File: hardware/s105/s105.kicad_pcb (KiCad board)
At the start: 2 copper layers, 86 x 159 mm, 367 parts, among them J1 Conn_01x06, P1 368255-2, Q1 BC847C, Q10 BC847C, Q11 BC847C, Q12 BC847C, Q13 BC847C, Q14 BC847C, Q15 BC847C, Q16 BC847C, Q17 BC847C, Q2 BC847C, Q20 BC847C, Q21 BC847C, Q22 BC847C, Q23 BC847C, Q3 BC847C, Q4 ., Q5 ., Q6 BC847C, Q7 BC847C, Q9 BC847C, U2 STM32F427VGT6, U4 case only, X1 8MHz 20pF

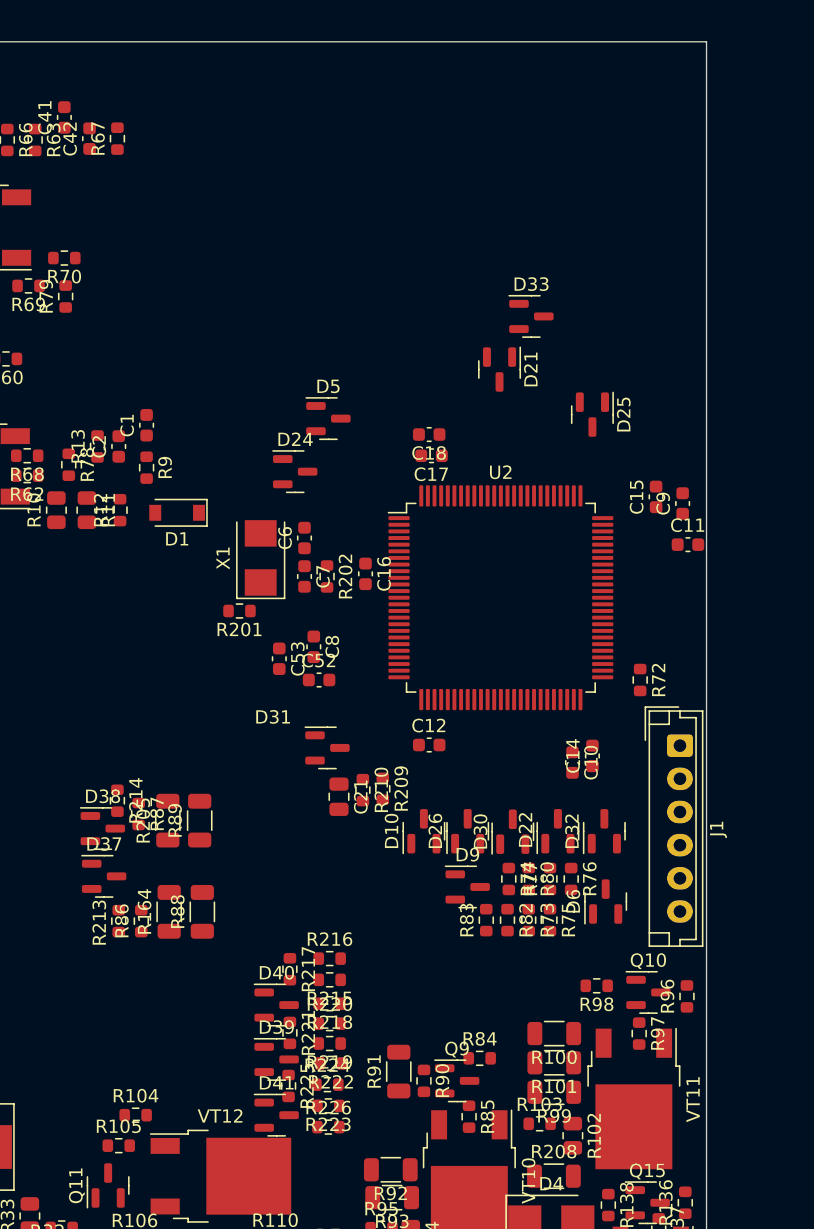
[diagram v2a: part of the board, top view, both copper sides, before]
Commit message: новые модули, продолжение расположения
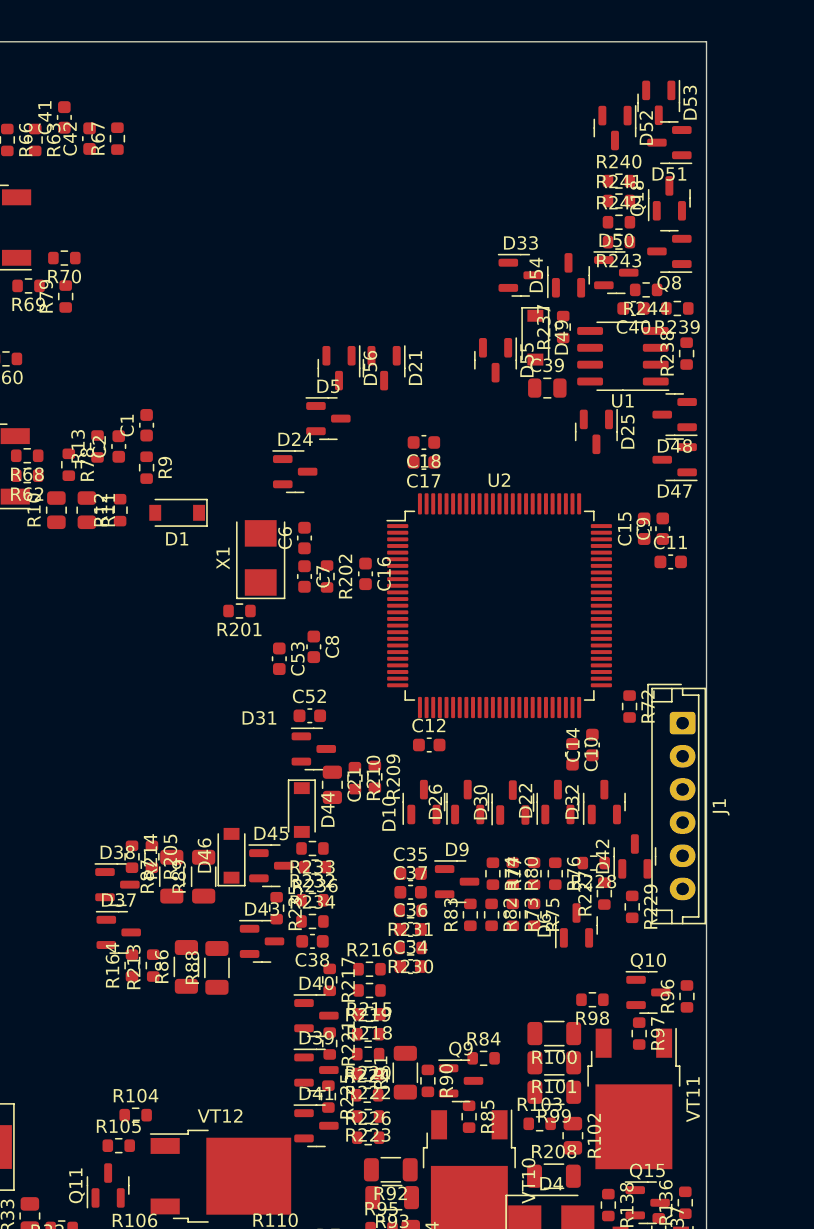
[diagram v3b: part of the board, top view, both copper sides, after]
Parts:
- added C34: 100nF, Capacitor_SMD:C_0603_1608Metric, F.Cu at (113.7, 169.7)
- added C35: 100nF, Capacitor_SMD:C_0603_1608Metric, F.Cu at (113.7, 162.7)
- added C36: 100nF, Capacitor_SMD:C_0603_1608Metric, F.Cu at (113.7, 166.9)
- added C37: 100nF, Capacitor_SMD:C_0603_1608Metric, F.Cu at (113.7, 164.1)
- added C38: 100nF, Capacitor_SMD:C_0603_1608Metric, F.Cu at (106.3, 167.8)
- added C39: C0805, Capacitor_SMD:C_0805_2012Metric, F.Cu at (124.0, 126.1)
- added C40: C0603, Capacitor_SMD:C_0603_1608Metric, F.Cu at (130.5, 120.1)
- added D42: BAV99, Package_TO_SOT_SMD:SOT-23, F.Cu at (130.6, 161.4)
- added D43: BAV99, Package_TO_SOT_SMD:SOT-23, F.Cu at (102.5, 167.8)
- added D44: 1N4148W, Diode_SMD:D_SOD-123, F.Cu at (105.5, 157.9)
- added D45: BAV99, Package_TO_SOT_SMD:SOT-23, F.Cu at (103.2, 162.1)
- added D46: 1N4148W, Diode_SMD:D_SOD-123, F.Cu at (100.2, 161.3)
- added D47: BAV99, Package_TO_SOT_SMD:SOT-23, F.Cu at (133.6, 131.5)
- added D48: BAV99, Package_TO_SOT_SMD:SOT-23, F.Cu at (133.6, 128.1)
- added D49: ., Diode_SMD:D_SOD-123, F.Cu at (123.1, 122.3)
- added D50: BAV99, Package_TO_SOT_SMD:SOT-23, F.Cu at (129.2, 117.4)
- added D51: BAV99, Package_TO_SOT_SMD:SOT-23, F.Cu at (133.2, 107.6)
- added D52: BAV99, Package_TO_SOT_SMD:SOT-23, F.Cu at (129.1, 106.5)
- added D53: BAV99, Package_TO_SOT_SMD:SOT-23, F.Cu at (132.4, 104.6)
- added D54: BAV99, Package_TO_SOT_SMD:SOT-23, F.Cu at (125.6, 117.6)
- added D55: BAV99, Package_TO_SOT_SMD:SOT-23, F.Cu at (120.1, 124.0)
- added D56: BAV99, Package_TO_SOT_SMD:SOT-23, F.Cu at (108.3, 124.6)
- added Q18: BC847C, Package_TO_SOT_SMD:SOT-23, F.Cu at (133.2, 111.8)
- added Q8: BC847C, Package_TO_SOT_SMD:SOT-23, F.Cu at (133.2, 115.8)
- added R227: NM, Resistor_SMD:R_0603_1608Metric, F.Cu at (128.3, 164.2)
- added R228: NM, Resistor_SMD:R_0603_1608Metric, F.Cu at (127.5, 161.9)
- added R229: NM, Resistor_SMD:R_0603_1608Metric, F.Cu at (130.4, 165.2)
- added R230: 3k, Resistor_SMD:R_0603_1608Metric, F.Cu at (113.7, 168.3)
- added R231: 3k, Resistor_SMD:R_0603_1608Metric, F.Cu at (113.7, 165.5)
- added R232: NM, Resistor_SMD:R_0603_1608Metric, F.Cu at (106.3, 164.7)
- added R233: 1k, Resistor_SMD:R_0603_1608Metric, F.Cu at (106.3, 160.8)
- added R234: NM, Resistor_SMD:R_0603_1608Metric, F.Cu at (106.3, 166.3)
- added R235: NM, Resistor_SMD:R_0603_1608Metric, F.Cu at (103.6, 165.3)
- added R236: 1k, Resistor_SMD:R_0603_1608Metric, F.Cu at (106.5, 162.2)
- added R237: 22k, Resistor_SMD:R_0603_1608Metric, F.Cu at (125.2, 121.5)
- added R238: NM, Resistor_SMD:R_0603_1608Metric, F.Cu at (134.5, 123.5)
- added R239: 4.7k, Resistor_SMD:R_0603_1608Metric, F.Cu at (133.8, 120.1)
- added R240: 47, Resistor_SMD:R_0603_1608Metric, F.Cu at (129.4, 110.5)
- added R241: 47, Resistor_SMD:R_0603_1608Metric, F.Cu at (129.4, 112.0)
- added R242: 51k, Resistor_SMD:R_0603_1608Metric, F.Cu at (129.4, 113.6)
- added R243: 33k, Resistor_SMD:R_0603_1608Metric, F.Cu at (129.4, 115.1)
- added R244: 33k, Resistor_SMD:R_0603_1608Metric, F.Cu at (131.4, 118.7)
- added U1: case only, Package_SO:SOIC-8_3.9x4.9mm_P1.27mm, F.Cu at (129.7, 123.7)
- R164, R205: value 3k -> 22k; footprint Resistor_SMD:R_1206_3216Metric -> Resistor_SMD:R_0603_1608Metric
- R201: value R0603 -> 3k
- R219: value 10k -> NM
- R220: value NM -> 10k
- R86, R87: value 22k -> 3k; footprint Resistor_SMD:R_0603_1608Metric -> Resistor_SMD:R_1206_3216Metric
- moved D21 8.70 mm to (111.7, 124.6)
- moved R87 5.35 mm to (95.7, 162.9), turned to 90 degrees
- moved R164 4.92 mm to (92.7, 169.6)
- moved R86 4.84 mm to (96.8, 169.7)
- moved R214 4.37 mm to (92.7, 161.4)
- moved R88 4.37 mm to (99.1, 169.8)
- moved D37 4.37 mm to (91.7, 167.1)
- moved D38 4.37 mm to (91.6, 163.5)
- moved R213 4.24 mm to (94.3, 169.6)
- moved R89 4.24 mm to (98.1, 162.9)
- moved R220 3.70 mm to (110.5, 176.3), turned to 180 degrees
- moved D33 3.20 mm to (122.0, 117.6)
- moved D39 3.10 mm to (106.6, 177.5)
- moved D40 3.10 mm to (106.6, 173.4)
- moved R215 3.10 mm to (110.6, 171.5)
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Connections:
- net /MCU/PC1 renamed /PC1
- C21 pad 1: /MCU/PB1 -> /PB1
- D24 pad 3: /MCU/PE3 -> /PE3
- D25 pad 3: /MCU/PA15 -> /PA15
- D30 pad 3: /MCU/PB10 -> /PB10
- D31 pad 3: /MCU/PB1 -> /PB1
- R164 pad 2: +3.3V -> /PA3
- R205 pad 1: +3.3V -> /CLT
- R205 pad 2: /CLT -> GND
- R209 pad 1: /MCU/PB1 -> /PB1
- R210 pad 1: /MCU/PB1 -> /PB1
- R213 pad 2: /PA3 -> GND
- R216 pad 2: +5V -> +5VD
- R219 pad 1: GND -> /TPS
- R219 pad 2: /TPS -> +5VD
- R220 pad 1: /TPS -> GND
- R220 pad 2: +5V -> /TPS
- R224 pad 2: +5V -> +5VD
- R72 pad 1: /MCU/PB15 -> /PB15
- R74 pad 1: +5V -> +5VD
- R80 pad 1: +5V -> +5VD
- R86 pad 2: GND -> +3.3V
- R87 pad 1: /CLT -> +3.3V
- R87 pad 2: GND -> /CLT
- U2 pad 15: /MCU/PC0 -> /PC0
- U2 pad 25: /MCU/PA2 -> /PA2
- U2 pad 38: /MCU/PE7 -> /PE7
- U2 pad 65: /MCU/PC8 -> /PC8
- U2 pad 68: /MCU/PA9 -> /PA9
- U2 pad 69: /MCU/PA10 -> /PA10

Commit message: заполняем плату дальше
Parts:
- added C44: C0603, Capacitor_SMD:C_0603_1608Metric, F.Cu at (86.6, 163.0)
- added C45: C0603, Capacitor_SMD:C_0603_1608Metric, F.Cu at (83.2, 173.6)
- added C46: C0603, Capacitor_SMD:C_0603_1608Metric, F.Cu at (80.9, 167.1)
- added C47: C0805, Capacitor_SMD:C_0805_2012Metric, F.Cu at (78.1, 161.1)
- added C48: C0603, Capacitor_SMD:C_0603_1608Metric, F.Cu at (71.5, 170.6)
- added C49: C0603, Capacitor_SMD:C_0603_1608Metric, F.Cu at (71.5, 169.2)
- added C50: C1206, Capacitor_SMD:C_1206_3216Metric, F.Cu at (72.3, 167.4)
- added C51: C1206, Capacitor_SMD:C_1206_3216Metric, F.Cu at (72.2, 163.8)
- added C55: C0603, Capacitor_SMD:C_0603_1608Metric, F.Cu at (71.4, 165.6)
- added C64: C0603, Capacitor_SMD:C_0603_1608Metric, F.Cu at (71.4, 160.2)
- added C69: 100nF, Capacitor_SMD:C_0603_1608Metric, F.Cu at (71.4, 158.8)
- added C70: C0603, Capacitor_SMD:C_0603_1608Metric, F.Cu at (71.4, 154.0)
- added C71: C0603, Capacitor_SMD:C_0603_1608Metric, F.Cu at (71.4, 152.6)
- added C72: 100nF, Capacitor_SMD:C_0603_1608Metric, F.Cu at (71.4, 151.3)
- added C73: C0603, Capacitor_SMD:C_0603_1608Metric, F.Cu at (71.4, 149.9)
- added C74: 100nF, Capacitor_SMD:C_0603_1608Metric, F.Cu at (73.8, 153.3)
- added C75: 100nF, Capacitor_SMD:C_0603_1608Metric, F.Cu at (71.4, 146.7)
- added C76: 100nF, Capacitor_SMD:C_0603_1608Metric, F.Cu at (73.0, 145.5)
- added C77: 100nF, Capacitor_SMD:C_0603_1608Metric, F.Cu at (71.4, 144.3)
- added C78: C0603, Capacitor_SMD:C_0603_1608Metric, F.Cu at (71.4, 143.0)
- added C79: 100nF, Capacitor_SMD:C_0603_1608Metric, F.Cu at (71.4, 141.8)
- added C80: C0603, Capacitor_SMD:C_0603_1608Metric, F.Cu at (71.4, 140.5)
- added C81: C0603, Capacitor_SMD:C_0603_1608Metric, F.Cu at (71.4, 139.2)
- added C82: C0603, Capacitor_SMD:C_0603_1608Metric, F.Cu at (73.8, 140.6)
- added C83: C0603, Capacitor_SMD:C_0603_1608Metric, F.Cu at (73.8, 143.5)
- added C84: C0603, Capacitor_SMD:C_0603_1608Metric, F.Cu at (71.4, 137.8)
- added C85: C0603, Capacitor_SMD:C_0603_1608Metric, F.Cu at (71.4, 136.5)
- added C86: C0603, Capacitor_SMD:C_0603_1608Metric, F.Cu at (71.4, 135.2)
- added C87: C0603, Capacitor_SMD:C_0603_1608Metric, F.Cu at (74.3, 133.9)
- added C88: C0603, Capacitor_SMD:C_0603_1608Metric, F.Cu at (73.8, 136.9)
- added C89: C0603, Capacitor_SMD:C_0603_1608Metric, F.Cu at (96.5, 146.7)
- added C90: C0603, Capacitor_SMD:C_0603_1608Metric, F.Cu at (103.7, 155.3)
- added C94: C0603, Capacitor_SMD:C_0603_1608Metric, F.Cu at (97.0, 158.4)
- added Q19: ., Package_TO_SOT_SMD:SOT-23, F.Cu at (76.4, 174.4)
- added R245: 4.7k, Resistor_SMD:R_0603_1608Metric, F.Cu at (85.7, 161.3)
- added R246: 82k, Resistor_SMD:R_0603_1608Metric, F.Cu at (80.4, 174.3)
- added R247: 4.7k, Resistor_SMD:R_0603_1608Metric, F.Cu at (78.5, 166.4)
- added R248: 10k, Resistor_SMD:R_0805_2012Metric, F.Cu at (79.9, 163.3)
- added R249: 10k, Resistor_SMD:R_0805_2012Metric, F.Cu at (78.6, 171.7)
- added R250: 10k, Resistor_SMD:R_0805_2012Metric, F.Cu at (76.4, 163.3)
- added R251: 4.7k, Resistor_SMD:R_0603_1608Metric, F.Cu at (76.9, 164.9)
- added R252: 4.7k, Resistor_SMD:R_0603_1608Metric, F.Cu at (78.7, 169.8)
- added R253: 4.7k, Resistor_SMD:R_0603_1608Metric, F.Cu at (77.0, 168.2)
- added R254: 4.7k, Resistor_SMD:R_0603_1608Metric, F.Cu at (90.5, 172.7)
- added R255: NM, Resistor_SMD:R_0603_1608Metric, F.Cu at (88.6, 172.7)
- added R256: 0, Resistor_SMD:R_0805_2012Metric, F.Cu at (71.7, 173.4)
- added R257: 0, Resistor_SMD:R_0805_2012Metric, F.Cu at (71.6, 161.8)
- added R258: 0, Resistor_SMD:R_0805_2012Metric, F.Cu at (71.6, 148.3)
- added R259: 0, Resistor_SMD:R_0805_2012Metric, F.Cu at (71.6, 155.5)
- added R260: 0, Resistor_SMD:R_0805_2012Metric, F.Cu at (71.6, 157.3)
- added R261: NM, Resistor_SMD:R_0603_1608Metric, F.Cu at (99.4, 146.6)
- added R262: MN, Resistor_SMD:R_0603_1608Metric, F.Cu at (98.6, 148.9)
- added R263: 3k, Resistor_SMD:R_0603_1608Metric, F.Cu at (98.0, 146.6)
- added R264: 3k, Resistor_SMD:R_0603_1608Metric, F.Cu at (96.4, 152.5)
- added R265: MN, Resistor_SMD:R_0603_1608Metric, F.Cu at (104.7, 148.5)
- added R266: MN, Resistor_SMD:R_0603_1608Metric, F.Cu at (100.8, 146.5)
- added R267: MN, Resistor_SMD:R_0603_1608Metric, F.Cu at (101.6, 148.9)
- added R268: MN, Resistor_SMD:R_0603_1608Metric, F.Cu at (102.3, 146.5)
- added R269: 10k, Resistor_SMD:R_0603_1608Metric, F.Cu at (100.0, 158.4)
- added R270: MN, Resistor_SMD:R_0603_1608Metric, F.Cu at (103.0, 158.4)
- added U3: case only, Package_SO:SOIC-8_3.9x4.9mm_P1.27mm, F.Cu at (85.4, 167.1)
- added U5: case only, Package_SO:SOIC-8_3.9x4.9mm_P1.27mm, F.Cu at (100.0, 154.1)
- moved C67 3.92 mm to (73.9, 171.1)
- moved C68 3.70 mm to (71.5, 171.9)
- moved C1 2.69 mm to (95.8, 127.1)
- moved D1 2.69 mm to (98.1, 133.7)
- moved R10 2.69 mm to (89.0, 133.5)
- moved R11 2.69 mm to (91.3, 133.5)
- moved R12 2.69 mm to (93.8, 133.5)
- moved R13 2.69 mm to (92.1, 128.7)
- moved R78 2.69 mm to (90.0, 130.1)
- moved R9 2.69 mm to (95.8, 130.3)
- moved C2 2.69 mm to (93.7, 128.7)
- moved C3 2.69 mm to (74.4, 127.6)
- moved VT23 2.69 mm to (81.7, 130.2)
- moved R62 2.69 mm to (86.8, 130.9)
- moved R68 2.69 mm to (86.8, 129.4)
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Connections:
- J1 pad 5: /MCU/5V -> +5V
- P1 pad 12: unconnected-(P1-Pad12) -> Net-(C48-Pad1)
- P1 pad 14: unconnected-(P1-Pad14) -> Net-(C55-Pad1)
- P1 pad 17: GND -> /GNDA
- P1 pad 20: GND -> /GNDA
- P1 pad 35: GND -> /GNDA
- P1 pad 36: GND -> /GNDA
- P1 pad 51: GND -> /GNDA
- P1 pad 52: GND -> /GNDA
- P1 pad 53: GND -> /GNDA
- P1 pad 54: GND -> /GNDA
- U2 pad 29: /MCU/PA4 -> /PA4
- U2 pad 47: /MCU/PB10 -> /PB10
- U2 pad 5: /MCU/PE6 -> /PE6

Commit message: +knock
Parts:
- added C91: C0603, Capacitor_SMD:C_0603_1608Metric, F.Cu at (83.3, 149.9)
- added C92: C0603, Capacitor_SMD:C_0603_1608Metric, F.Cu at (78.1, 151.0)
- added C95: C0603, Capacitor_SMD:C_0603_1608Metric, F.Cu at (80.6, 155.3)
- added C96: C0603, Capacitor_SMD:C_0603_1608Metric, F.Cu at (79.2, 158.1)
- added C97: C0603, Capacitor_SMD:C_0603_1608Metric, F.Cu at (79.2, 159.6)
- added C98: C0603, Capacitor_SMD:C_0603_1608Metric, F.Cu at (77.0, 155.3)
- added C99: C0603, Capacitor_SMD:C_0603_1608Metric, F.Cu at (88.3, 158.9)
- added D57: BAV99, Package_TO_SOT_SMD:SOT-23, F.Cu at (95.2, 156.3)
- added R271: 6k, Resistor_SMD:R_0603_1608Metric, F.Cu at (80.7, 151.9)
- added R272: 1k, Resistor_SMD:R_0603_1608Metric, F.Cu at (94.3, 149.1)
- added R273: 1k, Resistor_SMD:R_0603_1608Metric, F.Cu at (80.7, 150.5)
- added R274: 22k, Resistor_SMD:R_0603_1608Metric, F.Cu at (83.2, 153.5)
- added R275: 22k, Resistor_SMD:R_0603_1608Metric, F.Cu at (80.6, 154.0)
- added R276: 1k, Resistor_SMD:R_0603_1608Metric, F.Cu at (80.7, 149.1)
- added R277: 22k, Resistor_SMD:R_0603_1608Metric, F.Cu at (80.7, 147.8)
- added R278: 1k, Resistor_SMD:R_0603_1608Metric, F.Cu at (80.0, 146.4)
- added R279: 1k, Resistor_SMD:R_0603_1608Metric, F.Cu at (81.5, 157.7)
- added R280: 300, Resistor_SMD:R_0603_1608Metric, F.Cu at (97.0, 159.8)
- added R281: 18k, Resistor_SMD:R_0603_1608Metric, F.Cu at (83.1, 159.3)
- added R282: 18k, Resistor_SMD:R_0603_1608Metric, F.Cu at (81.5, 160.9)
- added R283: 300, Resistor_SMD:R_0603_1608Metric, F.Cu at (75.8, 159.6)
- added R284: 51k, Resistor_SMD:R_0603_1608Metric, F.Cu at (75.8, 158.3)
- added R285: 22k, Resistor_SMD:R_0603_1608Metric, F.Cu at (75.0, 156.1)
- added R286: 22k, Resistor_SMD:R_0603_1608Metric, F.Cu at (85.1, 158.9)
- added R287: 22k, Resistor_SMD:R_0603_1608Metric, F.Cu at (92.7, 152.9)
- added R288: 22k, Resistor_SMD:R_0603_1608Metric, F.Cu at (92.7, 156.1)
- added R289: 22k, Resistor_SMD:R_0603_1608Metric, F.Cu at (94.3, 150.7)
- added R290: 22k, Resistor_SMD:R_0603_1608Metric, F.Cu at (92.2, 149.9)
- added U6: LM2902, Package_SO:SO-14_3.9x8.65mm_P1.27mm, F.Cu at (87.6, 153.1)
- R153, R233, R236: value 1k -> 100
- R158: value 47k -> 4.7k
- R204, R80: value 1K -> 100
- R211, R215, R220, R269: value 10k -> 1k
- R218, R222: value 60k -> 6k
- R264: value 3k -> 300
- R60, R62, R69, R78, R79, R81: value 100 -> 10
- R72: value R0603 -> 1k
- moved D34 0.71 mm to (103.0, 238.1), turned to 0 degrees
- moved R264 0.20 mm to (96.2, 152.5)
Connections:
- J1 pad 5: +5V -> /MCU/5V
- R254 pad 1: +5V -> /MCU/5V

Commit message: can, analog inputs
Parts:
- removed C13: 10nF, Capacitor_SMD:C_0603_1608Metric
- added C100: C0603, Capacitor_SMD:C_0603_1608Metric, F.Cu at (79.3, 139.4)
- added C101: 100nF, Capacitor_SMD:C_0603_1608Metric, F.Cu at (93.4, 139.5)
- added C102: NM, Capacitor_SMD:C_0603_1608Metric, F.Cu at (88.9, 139.5)
- added C103: NM, Capacitor_SMD:C_0603_1608Metric, F.Cu at (84.1, 139.5)
- added C104: 100nF, Capacitor_SMD:C_0603_1608Metric, F.Cu at (97.5, 142.8)
- added C93: C0603, Capacitor_SMD:C_0603_1608Metric, F.Cu at (91.8, 148.1)
- added D58: BAV99, Package_TO_SOT_SMD:SOT-23, F.Cu at (80.6, 143.9)
- added D59: BAV99, Package_TO_SOT_SMD:SOT-23, F.Cu at (83.9, 143.5)
- added D60: BAV99, Package_TO_SOT_SMD:SOT-23, F.Cu at (87.3, 143.5)
- added D61: BAV99, Package_TO_SOT_SMD:SOT-23, F.Cu at (91.0, 143.5)
- added D62: NM, Diode_SMD:D_SOD-123, F.Cu at (97.5, 140.6)
- added Q24: ., Package_TO_SOT_SMD:SOT-23, F.Cu at (77.6, 148.8)
- added R291: 62, Resistor_SMD:R_0603_1608Metric, F.Cu at (82.5, 149.2)
- added R292: 62, Resistor_SMD:R_0603_1608Metric, F.Cu at (81.1, 147.6)
- added R293: NM, Resistor_SMD:R_0603_1608Metric, F.Cu at (75.3, 144.4)
- added R294: 51k, Resistor_SMD:R_0603_1608Metric, F.Cu at (77.0, 142.2)
- added R295: 4.7k, Resistor_SMD:R_0603_1608Metric, F.Cu at (78.5, 143.8)
- added R296: 33k, Resistor_SMD:R_0603_1608Metric, F.Cu at (79.3, 140.7)
- added R297: NM, Resistor_SMD:R_1206_3216Metric, F.Cu at (78.5, 135.6)
- added R298: 4.7k, Resistor_SMD:R_1206_3216Metric, F.Cu at (78.5, 137.7)
- added R299: NM, Resistor_SMD:R_0603_1608Metric, F.Cu at (81.9, 140.1)
- added R300: NM, Resistor_SMD:R_1206_3216Metric, F.Cu at (83.4, 135.6)
- added R301: NM, Resistor_SMD:R_1206_3216Metric, F.Cu at (83.4, 137.7)
- added R302: NM, Resistor_SMD:R_1206_3216Metric, F.Cu at (97.6, 138.4)
- added R303: 300, Resistor_SMD:R_0603_1608Metric, F.Cu at (84.1, 141.0)
- added R305: 300, Resistor_SMD:R_0603_1608Metric, F.Cu at (88.9, 141.0)
- added R306: NM, Resistor_SMD:R_0603_1608Metric, F.Cu at (86.7, 140.2)
- added R307: NM, Resistor_SMD:R_1206_3216Metric, F.Cu at (88.2, 135.6)
- added R308: NM, Resistor_SMD:R_1206_3216Metric, F.Cu at (88.2, 137.7)
- added R309: 33k, Resistor_SMD:R_0603_1608Metric, F.Cu at (93.3, 141.2)
- added R310: 51k, Resistor_SMD:R_0603_1608Metric, F.Cu at (91.3, 140.3)
- added R311: 4.7k, Resistor_SMD:R_1206_3216Metric, F.Cu at (92.9, 135.6)
- added R312: NM, Resistor_SMD:R_1206_3216Metric, F.Cu at (92.9, 137.7)
- added U7: SIT1042T/3, Package_SO:SOIC-8_3.9x4.9mm_P1.27mm, F.Cu at (87.3, 148.0)
- C48, C73, C78, C88: value C0603 -> 100nF
- R15: value 10K -> 51K
- moved R15 96.3 mm to (76.6, 146.6), turned to -90 degrees
- moved R14 84.2 mm to (97.3, 146.3), turned to -90 degrees
- moved C5 79.1 mm to (98.6, 146.3), turned to -90 degrees
- moved D38 5.51 mm to (92.2, 169.0)
- moved R213 5.51 mm to (94.9, 175.1)
- moved R86 5.51 mm to (97.4, 175.2)
- moved R88 5.51 mm to (99.7, 175.3)
- moved R89 5.51 mm to (98.7, 168.4)
- moved D37 5.51 mm to (92.3, 172.6)
- moved R164 5.51 mm to (93.3, 175.1)
- moved R205 5.51 mm to (94.8, 166.9)
- moved R214 5.51 mm to (93.3, 166.9)
- moved R87 5.51 mm to (96.3, 168.4)
- moved C39 5.26 mm to (124.1, 131.4)
- moved D48 5.26 mm to (133.7, 133.4)
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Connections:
- net /MCU/BOOT0 renamed /BOOT0
- C48 pad 1: Net-(C48-Pad1) -> GND
- C48 pad 2: GND -> /NEW_PIN
- C73 pad 1: /DCNS -> GND
- C73 pad 2: GND -> /DCNS
- C78 pad 1: /Speed_in -> GND
- C78 pad 2: GND -> /Speed_in
- C88 pad 1: /CAM_in -> GND
- C88 pad 2: GND -> /CAM_in
- P1 pad 12: Net-(C48-Pad1) -> /NEW_PIN
- U2 pad 48: /MCU/PB11 -> /PB11
- U2 pad 6: Net-(U2-Pad6) -> /VBAT
- U2 pad 7: /MCU/PC13 -> /PC13
- U2 pad 70: /MCU/PA11 -> /PA11
- U2 pad 71: /MCU/PA12 -> /PA12
- U2 pad 86: /MCU/PD5 -> /PD5
- U2 pad 89: /MCU/PB3 -> /PB3
